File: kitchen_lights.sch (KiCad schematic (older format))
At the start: 72 parts, among them IC1 ATTINY24/44/84-SSU, IC2 MBI5168, IC3 7805MS, P1 CONN_8, P2 CONN_8, P4 CONN_6, P5 CONN_6, P6 CONN_6, SW1 LPH_SW, SW2 LPH_SW, SW3 LPH_SW

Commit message: Some reworking...
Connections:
- wire segments 203 -> 179
- no-connect marks 8 -> 20
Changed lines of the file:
@@
-EESchema Schematic File Version 2  date Wed 04 May 2011 07:45:14 PM CEST
+EESchema Schematic File Version 2  date Wed 04 May 2011 08:11:15 PM CEST
 LIBS:power
 LIBS:device
@@
 Comment4 ""
 $EndDescr
+NoConn ~ 3950 3400
+NoConn ~ 3950 3500
+NoConn ~ 3950 3600
+NoConn ~ 3950 3700
+NoConn ~ 3950 3800
+NoConn ~ 3950 3900
+NoConn ~ 4450 3900
+NoConn ~ 4450 3800
+NoConn ~ 4450 3700
+NoConn ~ 4450 3600
+NoConn ~ 4450 3500
+NoConn ~ 4450 3400
+$Comp
+L CONN_6 P4
+U 1 1 4D84E524
+P 4300 3650
+F 0 "P4" V 4250 3650 60  0000 C CNN
+F 1 "CONN_6" V 4350 3650 60  0000 C CNN
+	1    4300 3650
+	1    0    0    -1
+$EndComp
 Wire Notes Line
 	3850 4100 6000 4100
@@
 Wire Wire Line
 	3700 5650 3250 5650
-Connection ~ 4450 3950
-Connection ~ 5450 3900
-Wire Wire Line
-	5450 3900 5450 3950
-Wire Wire Line
-	5450 3950 3950 3950
-Connection ~ 3950 3950
-Wire Wire Line
-	4450 3950 4450 3900
-Connection ~ 4450 3850
-Connection ~ 5450 3800
-Wire Wire Line
-	5450 3800 5450 3850
-Connection ~ 3950 3850
-Wire Wire Line
-	4450 3850 4450 3800
-Connection ~ 4450 3750
-Wire Wire Line
-	4450 3700 4450 3750
-Wire Wire Line
-	3950 3700 3950 3750
-Wire Wire Line
-	4450 3650 4450 3600
-Connection ~ 5450 3600
-Wire Wire Line
-	5450 3600 5450 3650
-Connection ~ 3950 3550
-Wire Wire Line
-	4450 3550 4450 3500
-Connection ~ 3950 3450
-Connection ~ 4450 3450
-Wire Wire Line
-	4450 3450 4450 3400
-Wire Wire Line
-	5450 3400 5450 3450
 Wire Wire Line
 	5500 3800 5400 3800
@@
 	5500 3900 5400 3900
 Wire Wire Line
-	3950 3400 3950 3450
-Wire Wire Line
-	3950 3500 3950 3550
-Connection ~ 4450 3550
-Wire Wire Line
 	5500 3400 5400 3400
-Connection ~ 5450 3400
-Wire Wire Line
-	5450 3500 5450 3550
-Connection ~ 5450 3500
-Connection ~ 4450 3650
-Wire Wire Line
-	3950 3600 3950 3650
-Connection ~ 3950 3650
-Connection ~ 3950 3750
-Wire Wire Line
-	5450 3700 5450 3750
-Connection ~ 5450 3700
-Wire Wire Line
-	3950 3800 3950 3850
-Wire Wire Line
-	3950 3950 3950 3900
 Wire Wire Line
 	3250 5750 3700 5750
@@
 Wire Notes Line
 	5400 5350 4350 5350
-Wire Wire Line
-	3950 3850 5450 3850
-Wire Wire Line
-	5450 3750 3950 3750
-Wire Wire Line
-	3950 3650 5450 3650
-Wire Wire Line
-	5450 3550 3950 3550
-Wire Wire Line
-	3950 3450 5450 3450
 Wire Notes Line
 	6000 3200 3850 3200
@@
 $EndComp
 $Comp
-L CONN_6 P4
-U 1 1 4D84E524
-P 4300 3650
-F 0 "P4" V 4250 3650 60  0000 C CNN
-F 1 "CONN_6" V 4350 3650 60  0000 C CNN
-	1    4300 3650
-	1    0    0    -1
-$EndComp
-$Comp

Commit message: Routed the V1.10 board. Still some silkscreen issues.
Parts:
- removed IC1: ATTINY24/44/84-SSU, attiny24_44_84-SOIC14, symbol ATTINY24/44/84-SSU
- removed P1, P2: CONN_8, symbol CONN_8
- removed P4, P5, P6: CONN_6, symbol CONN_6
- removed R2, R3, R4, R5, R6, R7, R8, R9: 10k, symbol R
- added IC1: MADW__ATTINY2313DIP/SO, symbol MADW__ATTINY2313DIP/SO
- added P1, P2: CONN_8X2, symbol CONN_8X2
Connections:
- net labels added: PB0, PB1, PB3, PD6, RXI, SW1, SW2, SW3, TXO
- net labels removed: PA0, PA1, PA2, PA3, SWITCHES
- wire segments 179 -> 174
- no-connect marks 20 -> 10
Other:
- moved on the sheet: C7, C8, D33, JP1, R1, R10, SW1, SW2, SW3

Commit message: Re-arranged the ATtiny2313 to let the MBI5168 have less vias.
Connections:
- net GNDPWR: no longer MH0.1, MH1.1, MH2.1, MH3.1, MH4.1, MH5.1, MH6.1, MH7.1
- no-connect marks 10 -> 18
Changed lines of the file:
@@
-EESchema Schematic File Version 2  date Fri 29 Jul 2011 03:02:18 AM CEST
+EESchema Schematic File Version 2  date Fri 29 Jul 2011 06:51:47 PM CEST
 LIBS:power
 LIBS:device
@@
 Sheet 1 1
 Title "BestKitchenLightsEver(tm)"
-Date "28 jul 2011"
-Rev "1.1"
+Date "29 jul 2011"
+Rev "1.10"
 Comp "My 2µF Blog"
 Comment1 ""
@@
 Comment4 ""
 $EndDescr
+NoConn ~ 3050 4000
+NoConn ~ 3050 3900
+NoConn ~ 3050 3800
+NoConn ~ 3050 3700
+NoConn ~ 3050 3600
+NoConn ~ 3050 3500
+NoConn ~ 3050 3400
+NoConn ~ 3050 3300
 Wire Wire Line
 	1550 5100 1950 5100
@@
 Wire Wire Line
 	5600 1450 5600 1400
-Connection ~ 3000 3900
-Wire Wire Line
-	3050 4000 3000 4000
-Wire Wire Line
-	3000 4000 3000 3600
 Wire Wire Line
 	5000 3600 5200 3600
@@
 Wire Notes Line
 	7250 6550 7250 1500
-Connection ~ 3000 3700
-Wire Wire Line
-	3000 3800 3050 3800
-Connection ~ 2850 3400
-Wire Wire Line
-	3050 3300 2850 3300
-Wire Wire Line
-	2850 3300 2850 3700
-Connection ~ 2850 3600
-Wire Wire Line
-	2850 3500 3050 3500
 Wire Wire Line
 	10500 2900 10500 2950
@@
 Wire Wire Line
 	10500 2450 10500 2500
-Wire Wire Line
-	2850 3600 3050 3600
-Wire Wire Line
-	2850 3400 3050 3400
-Connection ~ 2850 3500
-Connection ~ 3000 3600
-Wire Wire Line
-	3000 3700 3050 3700
 Wire Notes Line
 	550  3150 550  550
@@
 Wire Notes Line
 	5450 3200 3850 3200
-Wire Wire Line
-	3000 3900 3050 3900
-Connection ~ 3000 3800
 Wire Wire Line
 	5600 1000 5600 950
@@
 	1    0    0    -1
 $EndComp
-$Comp
-L GNDPWR #PWR05
-U 1 1 4D7ED608
-P 2850 3700
-F 0 "#PWR05" H 2850 3750 40  0001 C CNN
-F 1 "GNDPWR" H 2850 3620 40  0000 C CNN
-	1    2850 3700
-	1    0    0    -1
-$EndComp

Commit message: Switched to high efficiency Nichia superflux leds.
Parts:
- removed D1, D10, D11, D12, D13, D14, D15, D16, D17, D18, D19, D2, D20, D21, D22, D23, D24, D25, D26, D27, D28, D29, D3, D30, D31, D32, D4, D5, D6, D7, D8, D9: LED, symbol LED
- added D1, D10, D11, D12, D13, D14, D15, D16, D17, D18, D19, D2, D20, D21, D22, D23, D24, D25, D26, D27, D28, D29, D3, D30, D31, D32, D4, D5, D6, D7, D8, D9: LED, symbol MADW__NICHIA_NSPWR70CS-K1
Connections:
- net OUT0: now also D4.1
- net OUT1: now also D8.1
- net OUT2: now also D12.1
- net OUT3: now also D16.1
- net OUT4: now also D20.1
- net OUT5: now also D24.1
- net OUT6: now also D28.1
- net OUT7: now also D32.1
- net V_LED: now also D1.2, D13.2, D17.2, D21.2, D25.2, D29.2, D5.2, D9.2
- new net: D1.4, D2.3
- new net: D2.4, D3.3
- new net: D3.4, D4.3
- new net: D7.4, D8.3
- new net: D6.4, D7.3
- new net: D5.4, D6.3
- new net: D13.4, D14.3
- new net: D14.4, D15.3
- new net: D15.4, D16.3
- new net: D11.4, D12.3
- new net: D10.4, D11.3
- new net: D10.3, D9.4
- new net: D25.4, D26.3
- new net: D26.4, D27.3
- new net: D27.4, D28.3
- new net: D31.4, D32.3
- new net: D30.4, D31.3
- new net: D29.4, D30.3
- new net: D21.4, D22.3
- new net: D22.4, D23.3
- new net: D23.4, D24.3
- new net: D19.4, D20.3
- new net: D18.4, D19.3
- new net: D17.4, D18.3
- no-connect marks 18 -> 82

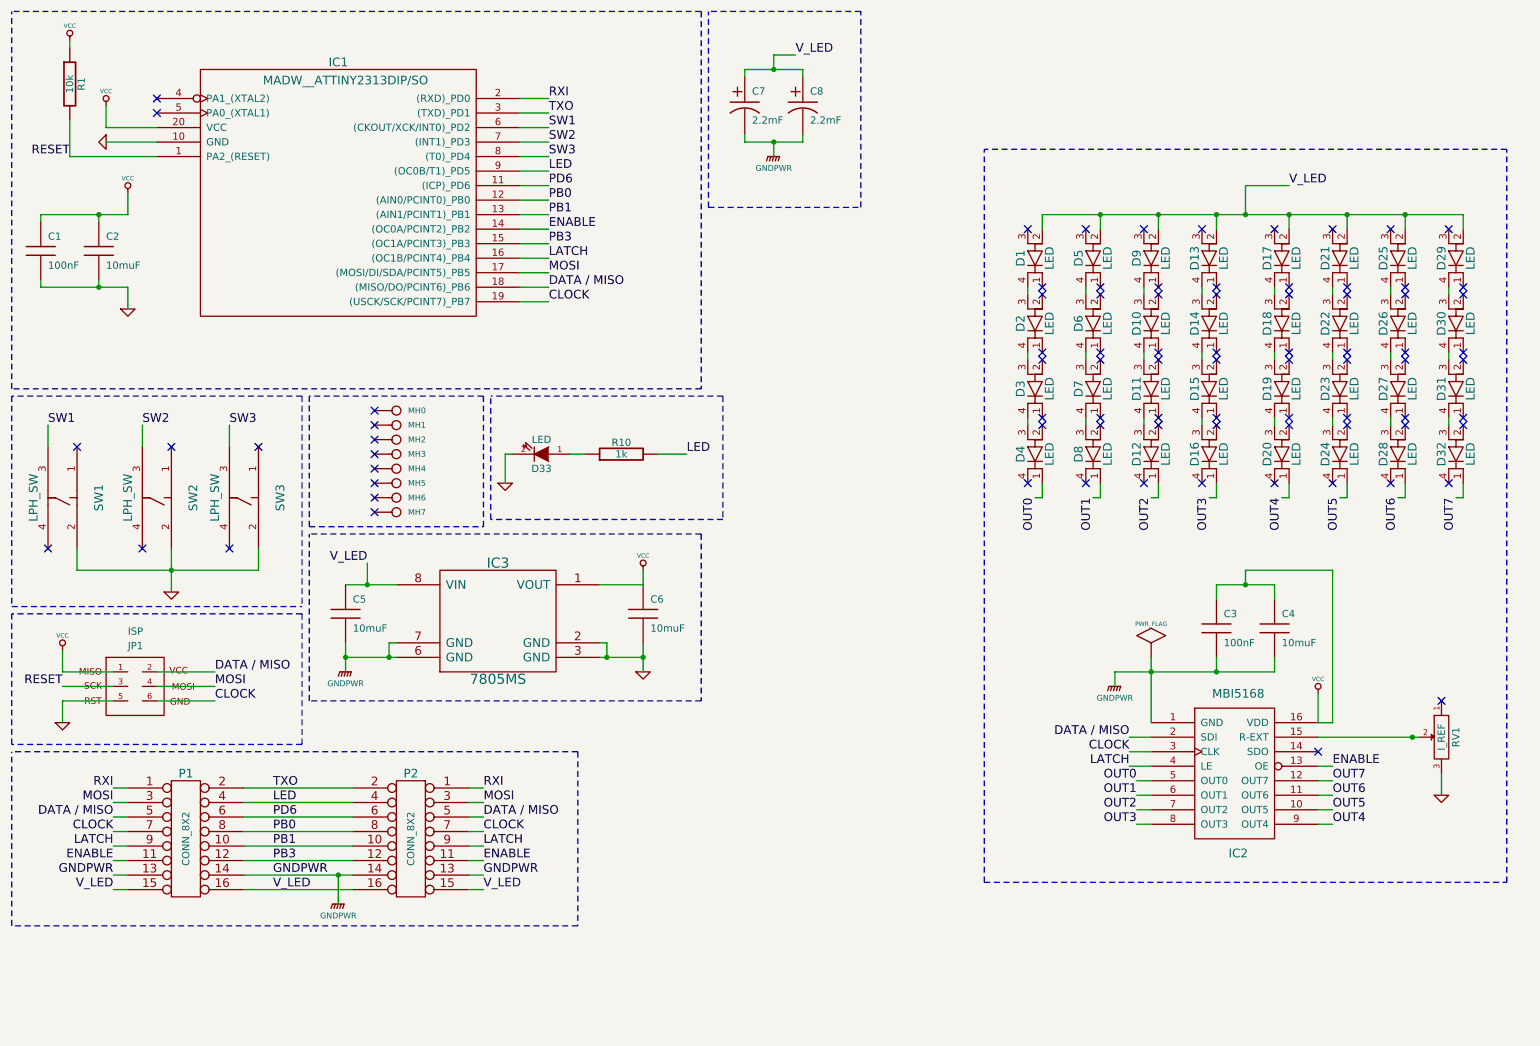
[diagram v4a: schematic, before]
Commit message: Used smaller electrolytics + 0603 resistors = smaller board.
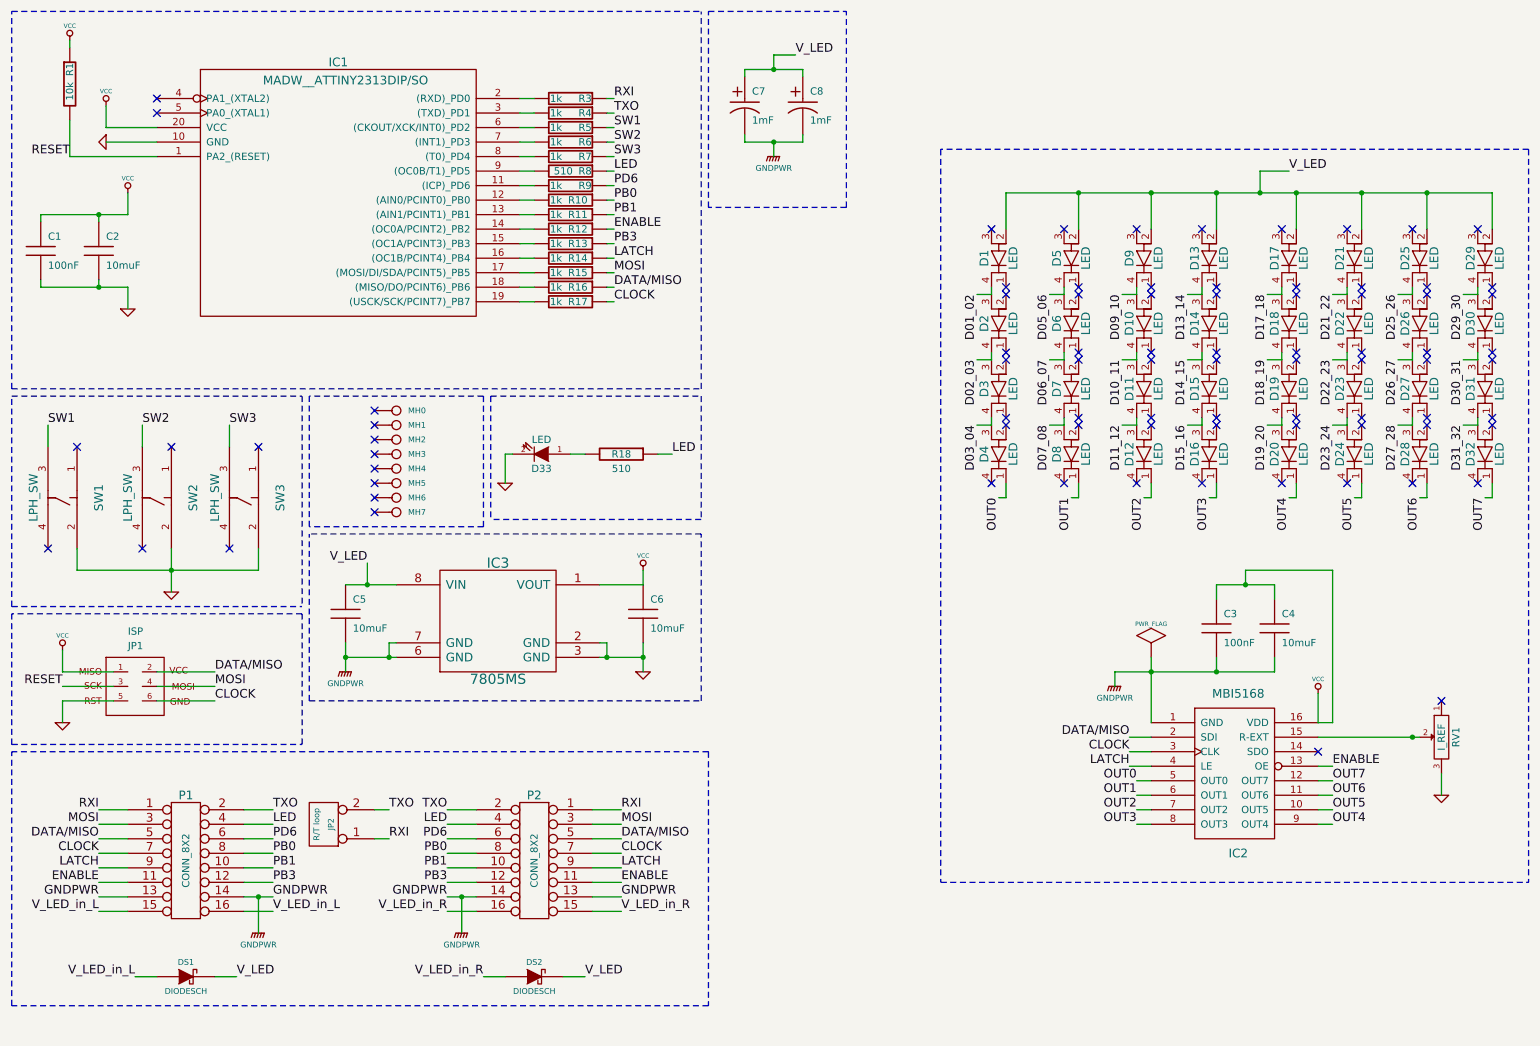
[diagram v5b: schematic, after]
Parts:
- added DS1, DS2: DIODESCH, symbol DIODESCH
- added JP2: R/T loop, symbol CONN_2
- added R11, R12, R13, R14, R15, R16, R17, R3, R4, R5, R6, R7, R9: 1k, symbol R
- added R18, R8: 510, symbol R
- C7, C8: value 2.2mF -> 1mF
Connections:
- net CLOCK: now also R17.1; no longer IC1.19 ((USCK/SCK/PCINT7)_PB7)
- net ENABLE: now also R12.1; no longer IC1.14 ((OC0A/PCINT2)_PB2)
- net LATCH: now also R14.1; no longer IC1.16 ((OC1B/PCINT4)_PB4)
- net LED: now also R18.1, R8.1; no longer IC1.9 ((OC0B/T1)_PD5), R10.2
- net MOSI: now also R15.1; no longer IC1.17 ((MOSI/DI/SDA/PCINT5)_PB5)
- net PB0: now also R10.1; no longer IC1.12 ((AIN0/PCINT0)_PB0)
- net PB1: now also R11.1; no longer IC1.13 ((AIN1/PCINT1)_PB1)
- net PB3: now also R13.1; no longer IC1.15 ((OC1A/PCINT3)_PB3)
- net PD6: now also R9.1; no longer IC1.11 ((ICP)_PD6)
- net RXI: now also JP2.1 (P1), R3.1; no longer IC1.2 ((RXD)_PD0)
- net SW1: now also R5.1; no longer IC1.6 ((CKOUT/XCK/INT0)_PD2)
- net SW2: now also R6.1; no longer IC1.7 ((INT1)_PD3)
- net SW3: now also R7.1; no longer IC1.8 ((T0)_PD4)
- net TXO: now also JP2.2 (PM), R4.1; no longer IC1.3 ((TXD)_PD1)
- net V_LED: now also DS1.2 (K), DS2.2 (K); no longer P1.15, P1.16, P2.15, P2.16
- net at D33.1 (A): now also R18.2; no longer R10.1
- net D01_02: now reaches D1.4, D2.3
- net D02_03: now reaches D2.4, D3.3
- net D03_04: now reaches D3.4, D4.3
- net D07_08: now reaches D7.4, D8.3
- net D06_07: now reaches D6.4, D7.3
- net D05_06: now reaches D5.4, D6.3
- net D13_14: now reaches D13.4, D14.3
- net D14_15: now reaches D14.4, D15.3
- net D15_16: now reaches D15.4, D16.3
- net D11_12: now reaches D11.4, D12.3
- net D10_11: now reaches D10.4, D11.3
- net D09_10: now reaches D10.3, D9.4
- net D25_26: now reaches D25.4, D26.3
- net D26_27: now reaches D26.4, D27.3
- net D27_28: now reaches D27.4, D28.3
- net D31_32: now reaches D31.4, D32.3
- net D30_31: now reaches D30.4, D31.3
- net D29_30: now reaches D29.4, D30.3
- net D21_22: now reaches D21.4, D22.3
- net D22_23: now reaches D22.4, D23.3
- net D23_24: now reaches D23.4, D24.3
- net D19_20: now reaches D19.4, D20.3
- net D18_19: now reaches D18.4, D19.3
- net D17_18: now reaches D17.4, D18.3
- net DATA / MISO renamed DATA/MISO
- net DATA/MISO: now also R16.1; no longer IC1.18 ((MISO/DO/PCINT6)_PB6)
- new net: IC1.11 ((ICP)_PD6), R9.2
- new net: IC1.12 ((AIN0/PCINT0)_PB0), R10.2
- new net: IC1.13 ((AIN1/PCINT1)_PB1), R11.2
- new net: IC1.14 ((OC0A/PCINT2)_PB2), R12.2
- new net: IC1.15 ((OC1A/PCINT3)_PB3), R13.2
- new net: IC1.16 ((OC1B/PCINT4)_PB4), R14.2
- new net: IC1.17 ((MOSI/DI/SDA/PCINT5)_PB5), R15.2
- new net: IC1.18 ((MISO/DO/PCINT6)_PB6), R16.2
- new net: IC1.19 ((USCK/SCK/PCINT7)_PB7), R17.2
- new net: IC1.2 ((RXD)_PD0), R3.2
- new net: IC1.3 ((TXD)_PD1), R4.2
- new net: IC1.6 ((CKOUT/XCK/INT0)_PD2), R5.2
- new net: IC1.7 ((INT1)_PD3), R6.2
- new net: IC1.8 ((T0)_PD4), R7.2
- new net: IC1.9 ((OC0B/T1)_PD5), R8.2
- new net V_LED_in_L: DS1.1 (A), P1.15, P1.16
- new net V_LED_in_R: DS2.1 (A), P2.15, P2.16
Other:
- moved on the sheet: D1, D10, D11, D12, D17, D18, D19, D2, D20, D21, D22, D23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
